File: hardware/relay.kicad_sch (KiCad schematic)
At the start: 0 parts

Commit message: power.kicad_sch düzenlemesi yapıldı.
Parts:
- added K1: Relay_SPDT, Relay_THT:Relay_SPDT_Omron-G5LE-1, symbol Relay:Relay_SPDT
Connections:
- new net COM: K1.11
- new net NC: K1.12
- new net NO: K1.14
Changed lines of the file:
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@@
 (kicad_sch (version 20230121) (generator eeschema)
   (paper "A4")
+  (wire (pts (xy 157.48 102.87) (xy 177.8 102.87))
+    (stroke (width 0) (type default))
+  )
+  (wire (pts (xy 160.02 85.09) (xy 160.02 82.55))
+    (stroke (width 0) (type default))
+  )
+  (wire (pts (xy 157.48 100.33) (xy 157.48 102.87))
+    (stroke (width 0) (type default))
+  )
+  (wire (pts (xy 154.94 85.09) (xy 154.94 80.01))
+    (stroke (width 0) (type default))
+  )
+  (wire (pts (xy 160.02 82.55) (xy 177.8 82.55))
+    (stroke (width 0) (type default))
+  )
+  (wire (pts (xy 154.94 80.01) (xy 177.8 80.01))
+    (stroke (width 0) (type default))
+  )
+  (hierarchical_label "COM" (shape input) (at 177.8 102.87 0) (fields_autoplaced)
+    (effects (font (size 1.27 1.27)) (justify left))
+  )
+  (hierarchical_label "NO" (shape output) (at 177.8 82.55 0) (fields_autoplaced)
+    (effects (font (size 1.27 1.27)) (justify left))
+  )
+  (hierarchical_label "NC" (shape output) (at 177.8 80.01 0) (fields_autoplaced)
+    (effects (font (size 1.27 1.27)) (justify left))
+  )
+  (symbol (lib_id "Relay:Relay_SPDT") (at 152.4 92.71 0) (unit 1)
+    (in_bom yes) (on_board yes) (dnp no) (fields_autoplaced)
+    (property "Reference" "K1" (at 163.83 91.44 0)
+      (effects (font (size 1.27 1.27)) (justify left))
+    )
+    (property "Value" "Relay_SPDT" (at 163.83 93.98 0)
+      (effects (font (size 1.27 1.27)) (justify left))
+    )
+    (property "Footprint" "Relay_THT:Relay_SPDT_Omron-G5LE-1" (at 163.83 93.98 0)
+      (effects (font (size 1.27 1.27)) (justify left) hide)
+    )
+    (property "Datasheet" "~" (at 152.4 92.71 0)
+      (effects (font (size 1.27 1.27)) hide)
+    )
+    (pin "11")
+    (pin "12")
+    (pin "14")
+    (pin "A1")
+    (pin "A2")
+    (instances
+      (project "drip-irrigation-sys-cc"
+        (path "/41708c1e-19b2-4374-83f2-108076d82b45/202a1cab-a33b-4ef0-945c-8042c7ebf8be"
+          (reference "K1") (unit 1)
+        )
+      )
+    )
+  )
 )

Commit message: Kicad şema düzenlemesi yapıldı.
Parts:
- added C14: 100nf, symbol Device:C
- added Q3: NPN, symbol Simulation_SPICE:NPN
- added R7: R, symbol Device:R
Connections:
- net at K1.A1: now also Q3.3 (E)
- net 5V_VCC: now reaches K1.A2
- new net: C14.2, Q3.2 (B)
- new net: C14.1, R7.2
- new net 5V_GND: Q3.1 (C)
- new net MCU_RELAY_PIN: R7.1
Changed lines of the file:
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@@
 (kicad_sch (version 20230121) (generator eeschema)
   (paper "A4")
+  (wire (pts (xy 106.68 62.23) (xy 113.03 62.23))
+    (stroke (width 0) (type default))
+  )
   (wire (pts (xy 157.48 102.87) (xy 177.8 102.87))
     (stroke (width 0) (type default))
   )
+  (wire (pts (xy 77.47 100.33) (xy 77.47 20.32))
+    (stroke (width 0) (type default))
+  )
   (wire (pts (xy 160.02 85.09) (xy 160.02 82.55))
+    (stroke (width 0) (type default))
+  )
+  (wire (pts (xy 106.68 27.94) (xy 106.68 62.23))
     (stroke (width 0) (type default))
   )
@@
     (stroke (width 0) (type default))
   )
+  (wire (pts (xy 146.05 67.31) (xy 146.05 85.09))
+    (stroke (width 0) (type default))
+  )
+  (wire (pts (xy 77.47 20.32) (xy 30.48 20.32))
+    (stroke (width 0) (type default))
+  )
+  (wire (pts (xy 30.48 24.13) (xy 146.05 24.13))
+    (stroke (width 0) (type default))
+  )
   (wire (pts (xy 160.02 82.55) (xy 177.8 82.55))
+    (stroke (width 0) (type default))
+  )
+  (wire (pts (xy 30.48 27.94) (xy 106.68 27.94))
+    (stroke (width 0) (type default))
+  )
+  (wire (pts (xy 133.35 62.23) (xy 138.43 62.23))
+    (stroke (width 0) (type default))
+  )
+  (wire (pts (xy 146.05 85.09) (xy 147.32 85.09))
+    (stroke (width 0) (type default))
+  )
+  (wire (pts (xy 120.65 62.23) (xy 125.73 62.23))
+    (stroke (width 0) (type default))
+  )
+  (wire (pts (xy 146.05 24.13) (xy 146.05 57.15))
+    (stroke (width 0) (type default))
+  )
+  (wire (pts (xy 147.32 100.33) (xy 77.47 100.33))
     (stroke (width 0) (type default))
   )
   (wire (pts (xy 154.94 80.01) (xy 177.8 80.01))
     (stroke (width 0) (type default))
+  )
+  (hierarchical_label "5V_VCC" (shape output) (at 30.48 20.32 180) (fields_autoplaced)
+    (effects (font (size 1.27 1.27)) (justify right))
+  )
+  (hierarchical_label "5V_GND" (shape output) (at 30.48 24.13 180) (fields_autoplaced)
+    (effects (font (size 1.27 1.27)) (justify right))
   )
   (hierarchical_label "COM" (shape input) (at 177.8 102.87 0) (fields_autoplaced)
@@
     (effects (font (size 1.27 1.27)) (justify left))
   )
+  (hierarchical_label "MCU_RELAY_PIN" (shape output) (at 30.48 27.94 180) (fields_autoplaced)
+    (effects (font (size 1.27 1.27)) (justify right))
+  )
   (hierarchical_label "NC" (shape output) (at 177.8 80.01 0) (fields_autoplaced)
     (effects (font (size 1.27 1.27)) (justify left))
   )
+  (symbol (lib_id "Simulation_SPICE:NPN") (at 143.51 62.23 0) (unit 1)
+    (in_bom yes) (on_board yes) (dnp no) (fields_autoplaced)
+    (property "Reference" "Q3" (at 148.59 60.96 0)
+      (effects (font (size 1.27 1.27)) (justify left))
+    )
+    (property "Value" "NPN" (at 148.59 63.5 0)
+      (effects (font (size 1.27 1.27)) (justify left))
+    )
+    (property "Footprint" "" (at 207.01 62.23 0)
+      (effects (font (size 1.27 1.27)) hide)
+    )
+    (property "Datasheet" "~" (at 207.01 62.23 0)
+      (effects (font (size 1.27 1.27)) hide)
+    )
+    (property "Sim.Device" "NPN" (at 143.51 62.23 0)
+      (effects (font (size 1.27 1.27)) hide)
+    )
+    (property "Sim.Type" "GUMMELPOON" (at 143.51 62.23 0)
+      (effects (font (size 1.27 1.27)) hide)
+    )
+    (property "Sim.Pins" "1=C 2=B 3=E" (at 143.51 62.23 0)
+      (effects (font (size 1.27 1.27)) hide)
+    )
+    (pin "1")
+    (pin "2")
+    (pin "3")
+    (instances
+      (project "drip-irrigation-sys-cc"
+        (path "/41708c1e-19b2-4374-83f2-108076d82b45/202a1cab-a33b-4ef0-945c-8042c7ebf8be"
+          (reference "Q3") (unit 1)
+        )
+      )
+    )
+  )
+  (symbol (lib_id "Device:R") (at 116.84 62.23 90) (unit 1)
+    (in_bom yes) (on_board yes) (dnp no) (fields_autoplaced)
+    (property "Reference" "R7" (at 116.84 55.88 90)
+      (effects (font (size 1.27 1.27)))
+    )
+    (property "Value" "R" (at 116.84 58.42 90)
+      (effects (font (size 1.27 1.27)))
+    )
+    (property "Footprint" "" (at 116.84 64.008 90)
+      (effects (font (size 1.27 1.27)) hide)
+    )
+    (property "Datasheet" "~" (at 116.84 62.23 0)
+      (effects (font (size 1.27 1.27)) hide)
+    )
+    (pin "1")
+    (pin "2")
+    (instances
+      (project "drip-irrigation-sys-cc"
+        (path "/41708c1e-19b2-4374-83f2-108076d82b45/202a1cab-a33b-4ef0-945c-8042c7ebf8be"
+          (reference "R7") (unit 1)
+        )
+      )
+    )
+  )
+  (symbol (lib_id "Device:C") (at 129.54 62.23 90) (unit 1)
+    (in_bom yes) (on_board yes) (dnp no) (fields_autoplaced)
+    (property "Reference" "C14" (at 129.54 54.61 90)
+      (effects (font (size 1.27 1.27)))
+    )
+    (property "Value" "100nf" (at 129.54 57.15 90)
+      (effects (font (size 1.27 1.27)))
+    )
+    (property "Footprint" "" (at 133.35 61.2648 0)
+      (effects (font (size 1.27 1.27)) hide)
+    )
+    (property "Datasheet" "~" (at 129.54 62.23 0)
+      (effects (font (size 1.27 1.27)) hide)
+    )
+    (pin "1")
+    (pin "2")
+    (instances
+      (project "drip-irrigation-sys-cc"
+        (path "/41708c1e-19b2-4374-83f2-108076d82b45/202a1cab-a33b-4ef0-945c-8042c7ebf8be"
+          (reference "C14") (unit 1)
+        )
+      )
+    )
+  )
   (symbol (lib_id "Relay:Relay_SPDT") (at 152.4 92.71 0) (unit 1)

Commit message: Kicad şema düzenlemesi yapıldı.
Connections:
- net 5V_GND renamed GND
- net 5V_VCC renamed +5V
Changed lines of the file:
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@@
 (kicad_sch (version 20230121) (generator eeschema)
   (paper "A4")
-  (wire (pts (xy 106.68 62.23) (xy 113.03 62.23))
+  (wire (pts (xy 104.14 62.23) (xy 113.03 62.23))
     (stroke (width 0) (type default))
   )
@@
     (stroke (width 0) (type default))
   )
-  (wire (pts (xy 77.47 100.33) (xy 77.47 20.32))
-    (stroke (width 0) (type default))
-  )
   (wire (pts (xy 160.02 85.09) (xy 160.02 82.55))
-    (stroke (width 0) (type default))
-  )
-  (wire (pts (xy 106.68 27.94) (xy 106.68 62.23))
     (stroke (width 0) (type default))
   )
@@
     (stroke (width 0) (type default))
   )
-  (wire (pts (xy 77.47 20.32) (xy 30.48 20.32))
+  (wire (pts (xy 153.67 24.13) (xy 146.05 24.13))
     (stroke (width 0) (type default))
   )
-  (wire (pts (xy 30.48 24.13) (xy 146.05 24.13))
+  (wire (pts (xy 132.08 101.6) (xy 147.32 101.6))
     (stroke (width 0) (type default))
   )
   (wire (pts (xy 160.02 82.55) (xy 177.8 82.55))
-    (stroke (width 0) (type default))
-  )
-  (wire (pts (xy 30.48 27.94) (xy 106.68 27.94))
     (stroke (width 0) (type default))
   )
@@
     (stroke (width 0) (type default))
   )
+  (wire (pts (xy 147.32 101.6) (xy 147.32 100.33))
+    (stroke (width 0) (type default))
+  )
   (wire (pts (xy 120.65 62.23) (xy 125.73 62.23))
     (stroke (width 0) (type default))
@@
     (stroke (width 0) (type default))
   )
-  (wire (pts (xy 147.32 100.33) (xy 77.47 100.33))
+  (wire (pts (xy 132.08 95.25) (xy 132.08 101.6))
     (stroke (width 0) (type default))
   )
@@
     (stroke (width 0) (type default))
   )
-  (hierarchical_label "5V_VCC" (shape output) (at 30.48 20.32 180) (fields_autoplaced)
-    (effects (font (size 1.27 1.27)) (justify right))
-  )
-  (hierarchical_label "5V_GND" (shape output) (at 30.48 24.13 180) (fields_autoplaced)
-    (effects (font (size 1.27 1.27)) (justify right))
+  (wire (pts (xy 153.67 31.75) (xy 153.67 24.13))
+    (stroke (width 0) (type default))
   )
   (hierarchical_label "COM" (shape input) (at 177.8 102.87 0) (fields_autoplaced)
@@
     (effects (font (size 1.27 1.27)) (justify left))
   )
-  (hierarchical_label "MCU_RELAY_PIN" (shape output) (at 30.48 27.94 180) (fields_autoplaced)
+  (hierarchical_label "MCU_RELAY_PIN" (shape output) (at 104.14 62.23 180) (fields_autoplaced)
     (effects (font (size 1.27 1.27)) (justify right))
   )
   (hierarchical_label "NC" (shape output) (at 177.8 80.01 0) (fields_autoplaced)
     (effects (font (size 1.27 1.27)) (justify left))
+  )
+  (symbol (lib_id "power:+5V") (at 132.08 95.25 0) (unit 1)
+    (in_bom yes) (on_board yes) (dnp no) (fields_autoplaced)
+    (property "Reference" "#PWR013" (at 132.08 99.06 0)
+      (effects (font (size 1.27 1.27)) hide)
+    )
+    (property "Value" "+5V" (at 132.08 90.17 0)
+      (effects (font (size 1.27 1.27)))
+    )
+    (property "Footprint" "" (at 132.08 95.25 0)
+      (effects (font (size 1.27 1.27)) hide)
+    )
+    (property "Datasheet" "" (at 132.08 95.25 0)
+      (effects (font (size 1.27 1.27)) hide)
+    )
+    (pin "1")
+    (instances
+      (project "drip-irrigation-sys-cc"
+        (path "/41708c1e-19b2-4374-83f2-108076d82b45/202a1cab-a33b-4ef0-945c-8042c7ebf8be"
+          (reference "#PWR013") (unit 1)
+        )
+      )
+    )
   )
   (symbol (lib_id "Simulation_SPICE:NPN") (at 143.51 62.23 0) (unit 1)
@@
         )
       )
+    )
+  )
+  (symbol (lib_id "power:GND") (at 153.67 31.75 0) (unit 1)
+    (in_bom yes) (on_board yes) (dnp no) (fields_autoplaced)
+    (property "Reference" "#PWR012" (at 153.67 38.1 0)
+      (effects (font (size 1.27 1.27)) hide)
+    )
+    (property "Value" "GND" (at 153.67 36.83 0)
+      (effects (font (size 1.27 1.27)))
+    )
+    (property "Footprint" "" (at 153.67 31.75 0)
+      (effects (font (size 1.27 1.27)) hide)
+    )
+    (property "Datasheet" "" (at 153.67 31.75 0)
+      (effects (font (size 1.27 1.27)) hide)
+    )
+    (pin "1")
+    (instances
+      (project "drip-irrigation-sys-cc"
+        (path "/41708c1e-19b2-4374-83f2-108076d82b45/202a1cab-a33b-4ef0-945c-8042c7ebf8be"
+          (reference "#PWR012") (unit 1)
+        )
+      )

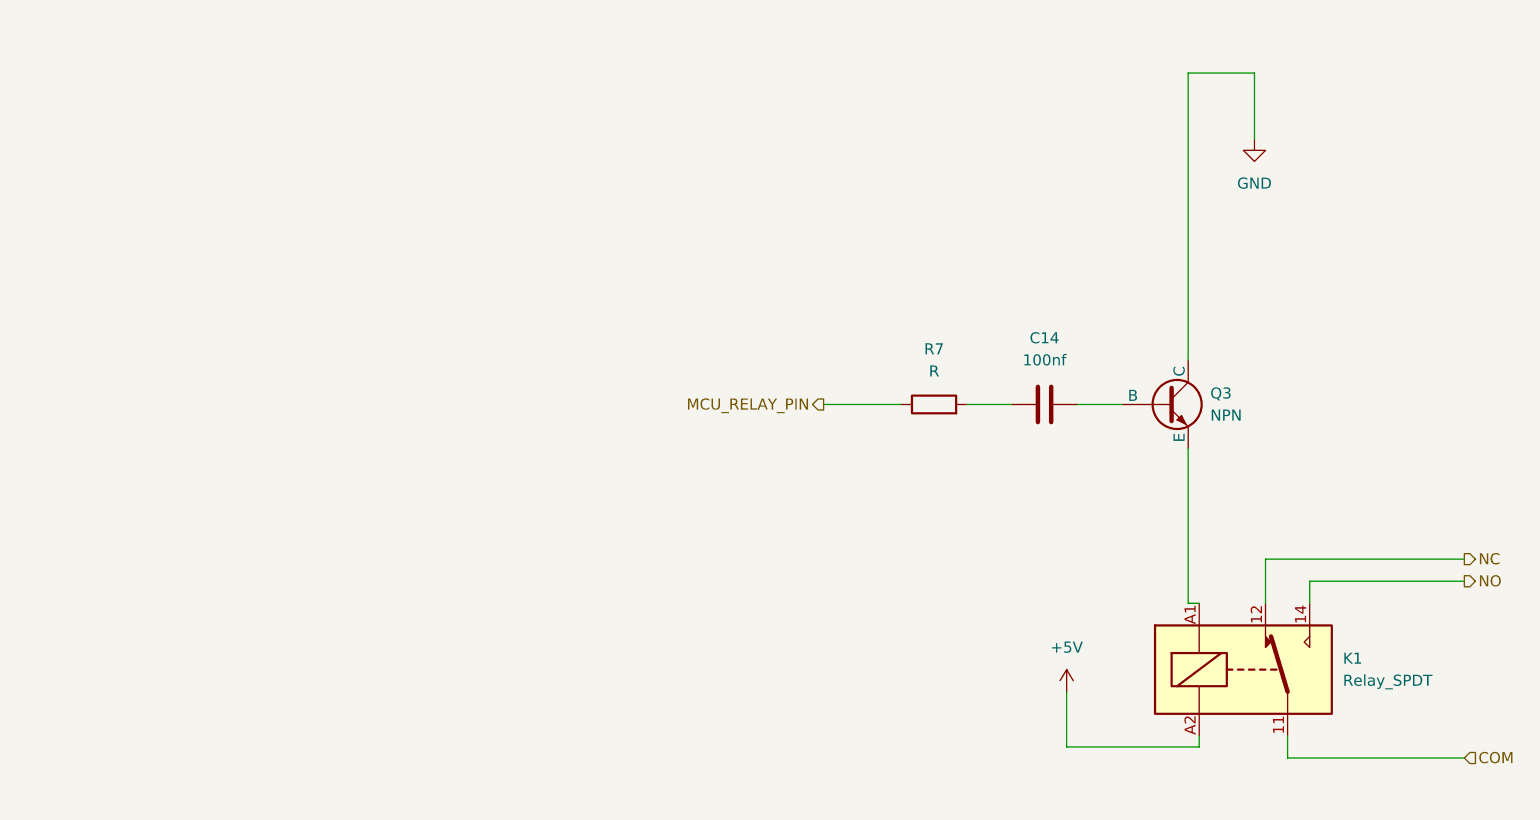
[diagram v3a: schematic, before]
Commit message: Kicad Power Modülü Tamamlandı.
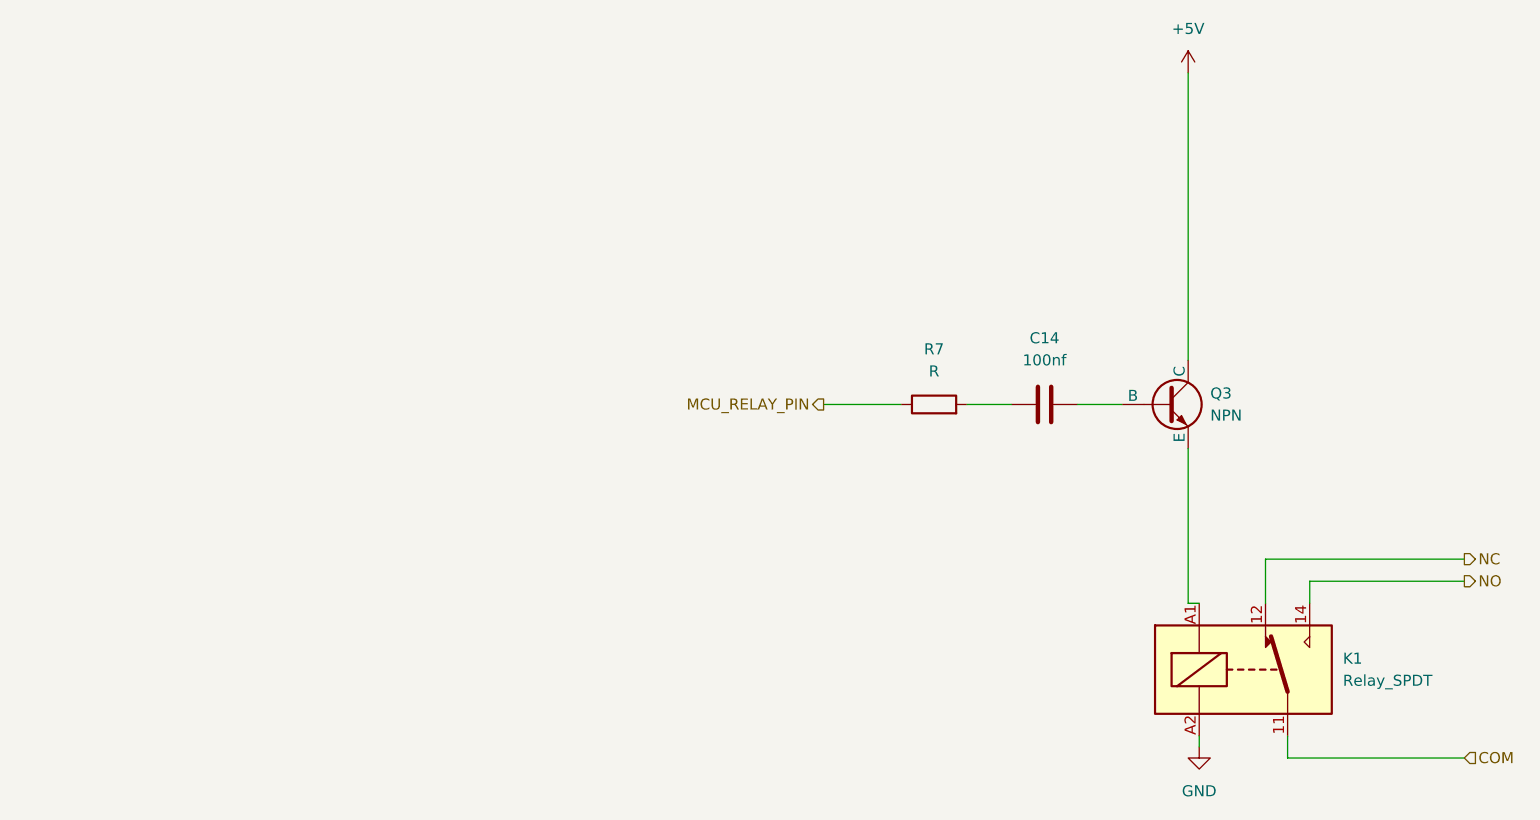
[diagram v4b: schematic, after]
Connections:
- net +5V: now also Q3.1 (C); no longer K1.A2
- net GND: now also K1.A2; no longer Q3.1 (C)
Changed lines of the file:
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@@
-    (stroke (width 0) (type default))
-  )
-  (wire (pts (xy 153.67 24.13) (xy 146.05 24.13))
-    (stroke (width 0) (type default))
-  )
-  (wire (pts (xy 132.08 101.6) (xy 147.32 101.6))
     (stroke (width 0) (type default))
   )
@@
     (stroke (width 0) (type default))
   )
-  (wire (pts (xy 132.08 95.25) (xy 132.08 101.6))
-    (stroke (width 0) (type default))
-  )
   (wire (pts (xy 154.94 80.01) (xy 177.8 80.01))
-    (stroke (width 0) (type default))
-  )
-  (wire (pts (xy 153.67 31.75) (xy 153.67 24.13))
     (stroke (width 0) (type default))
   )
@@
     (effects (font (size 1.27 1.27)) (justify left))
   )
-  (symbol (lib_id "power:+5V") (at 132.08 95.25 0) (unit 1)
+  (symbol (lib_id "power:+5V") (at 146.05 24.13 0) (unit 1)
     (in_bom yes) (on_board yes) (dnp no) (fields_autoplaced)
-    (property "Reference" "#PWR013" (at 132.08 99.06 0)
+    (property "Reference" "#PWR013" (at 146.05 27.94 0)
       (effects (font (size 1.27 1.27)) hide)
     )
-    (property "Value" "+5V" (at 132.08 90.17 0)
+    (property "Value" "+5V" (at 146.05 19.05 0)
       (effects (font (size 1.27 1.27)))
     )
-    (property "Footprint" "" (at 132.08 95.25 0)
+    (property "Footprint" "" (at 146.05 24.13 0)
       (effects (font (size 1.27 1.27)) hide)
     )
-    (property "Datasheet" "" (at 132.08 95.25 0)
+    (property "Datasheet" "" (at 146.05 24.13 0)
       (effects (font (size 1.27 1.27)) hide)
     )
@@
     )
   )
-  (symbol (lib_id "power:GND") (at 153.67 31.75 0) (unit 1)
+  (symbol (lib_id "power:GND") (at 147.32 101.6 0) (unit 1)
     (in_bom yes) (on_board yes) (dnp no) (fields_autoplaced)
-    (property "Reference" "#PWR012" (at 153.67 38.1 0)
+    (property "Reference" "#PWR012" (at 147.32 107.95 0)
       (effects (font (size 1.27 1.27)) hide)
     )
-    (property "Value" "GND" (at 153.67 36.83 0)
+    (property "Value" "GND" (at 147.32 106.68 0)
       (effects (font (size 1.27 1.27)))
     )
-    (property "Footprint" "" (at 153.67 31.75 0)
+    (property "Footprint" "" (at 147.32 101.6 0)
       (effects (font (size 1.27 1.27)) hide)
     )
-    (property "Datasheet" "" (at 153.67 31.75 0)
+    (property "Datasheet" "" (at 147.32 101.6 0)
       (effects (font (size 1.27 1.27)) hide)
     )

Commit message: Kicad şema düzenlemesi yapıldı.
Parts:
- C14: footprint (none) -> Capacitor_SMD:C_0201_0603Metric; Digikey (none) -> 490-3167-2-ND
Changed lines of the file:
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@@
       (effects (font (size 1.27 1.27)))
     )
-    (property "Footprint" "" (at 133.35 61.2648 0)
+    (property "Footprint" "Capacitor_SMD:C_0201_0603Metric" (at 133.35 61.2648 0)
       (effects (font (size 1.27 1.27)) hide)
     )
@@
       (effects (font (size 1.27 1.27)) hide)
     )
+    (property "Digikey" "490-3167-2-ND" (at 129.54 62.23 0)
+      (effects (font (size 1.27 1.27)) hide)
+    )
